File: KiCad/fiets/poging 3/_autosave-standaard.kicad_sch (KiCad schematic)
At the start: 32 parts, among them J1 Conn_01x04_Female, J2 R pinnen RGB strips, J3 282837-4, J4 282841-2, J5 282841-2, SW1 ENABLE, SW2 BOOT, U1 ESP32-WROOM-32E_(16MB), U2 AMS1117

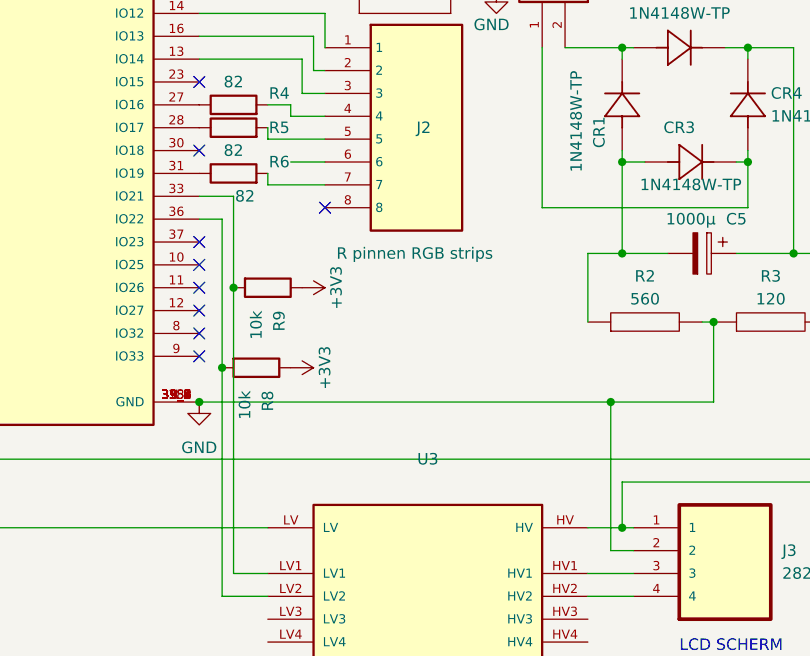
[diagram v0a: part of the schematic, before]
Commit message: kicad fiets hertekend
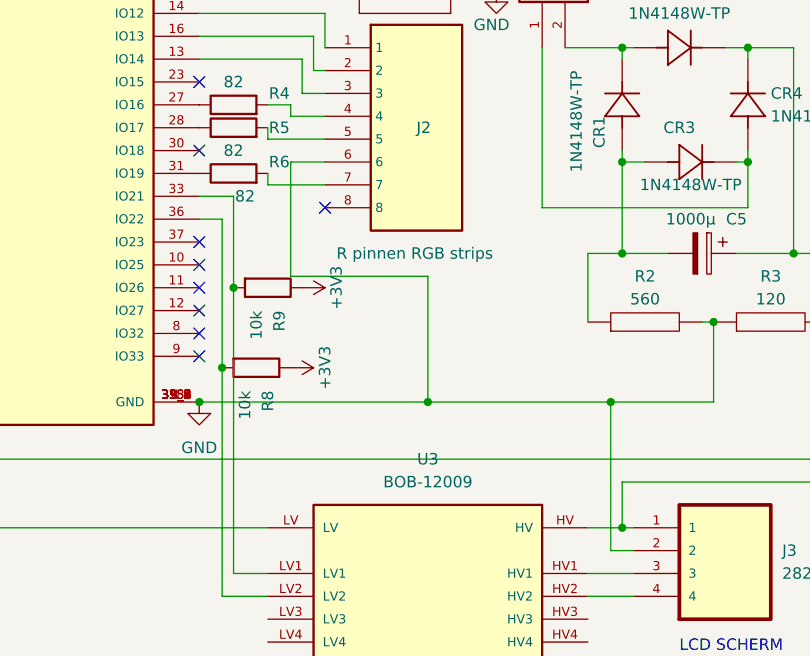
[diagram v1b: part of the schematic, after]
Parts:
- C2: footprint (none) -> libraries:CAP_EEE0JA101WR
- U3: value (none) -> BOB-12009; footprint (none) -> BOB-12009:CONV_BOB-12009
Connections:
- net GND: now also J2.6
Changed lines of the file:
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@@
   (junction (at 118.11 64.77) (diameter 0) (color 0 0 0 0)
+  )
+  (junction (at 137.16 115.57) (diameter 0) (color 0 0 0 0)
   )
   (junction (at 158.75 34.29) (diameter 0) (color 0 0 0 0)
@@
     (stroke (width 0) (type default) (color 0 0 0 0))
   )
+  (wire (pts (xy 137.16 115.57) (xy 157.48 115.57))
+    (stroke (width 0) (type default) (color 0 0 0 0))
+  )
   (wire (pts (xy 71.12 87.63) (xy 71.12 83.82))
     (stroke (width 0) (type default) (color 0 0 0 0))
@@
     (stroke (width 0) (type default) (color 0 0 0 0))
   )
+  (wire (pts (xy 121.92 88.9) (xy 121.92 101.6))
+    (stroke (width 0) (type default) (color 0 0 0 0))
+  )
   (wire (pts (xy 125.73 88.9) (xy 121.92 88.9))
     (stroke (width 0) (type default) (color 0 0 0 0))
@@
     (stroke (width 0) (type default) (color 0 0 0 0))
   )
+  (wire (pts (xy 121.92 101.6) (xy 137.16 101.6))
+    (stroke (width 0) (type default) (color 0 0 0 0))
+  )
   (wire (pts (xy 57.15 121.92) (xy 57.15 80.01))
     (stroke (width 0) (type default) (color 0 0 0 0))
@@
     (stroke (width 0) (type default) (color 0 0 0 0))
   )
-  (wire (pts (xy 111.76 115.57) (xy 157.48 115.57))
+  (wire (pts (xy 111.76 115.57) (xy 137.16 115.57))
     (stroke (width 0) (type default) (color 0 0 0 0))
   )
@@
   )
   (wire (pts (xy 118.11 64.77) (xy 124.46 64.77))
+    (stroke (width 0) (type default) (color 0 0 0 0))
+  )
+  (wire (pts (xy 137.16 101.6) (xy 137.16 115.57))
     (stroke (width 0) (type default) (color 0 0 0 0))
   )
@@
       (effects (font (size 1.27 1.27)) (justify right))
     )
-    (property "Footprint" "" (id 2) (at 115.8748 43.18 0)
+    (property "Footprint" "libraries:CAP_EEE0JA101WR" (id 2) (at 115.8748 43.18 0)
       (effects (font (size 1.27 1.27)) hide)
     )
@@
     (in_bom yes) (on_board yes) (fields_autoplaced)
     (property "Reference" "U3" (id 0) (at 137.16 121.92 0))
-    (property "Value" "" (id 1) (at 137.16 124.46 0))
-    (property "Footprint" "" (id 2) (at 137.16 137.16 0)
-      (effects (font (size 1.27 1.27)) (justify left bottom) hide)
-    )
+    (property "Value" "BOB-12009" (id 1) (at 137.16 124.46 0))
+    (property "Footprint" "BOB-12009:CONV_BOB-12009" (id 2) (at 137.16 137.16 0)
+      (effects (font (size 1.27 1.27)) (justify left bottom) hide)
+    )
